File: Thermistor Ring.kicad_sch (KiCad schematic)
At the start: 20 parts, among them IC1 MAX30210ENL+, IC2 MAX30210ENL+, IC3 MAX30210ENL+, IC4 MAX30210ENL+, IC5 MAX30210ENL+, IC6 MAX30210ENL+, J1 Conn_01x04_Socket, J3 Conn_01x03_Socket, U1 TPS7A2018PDBVR

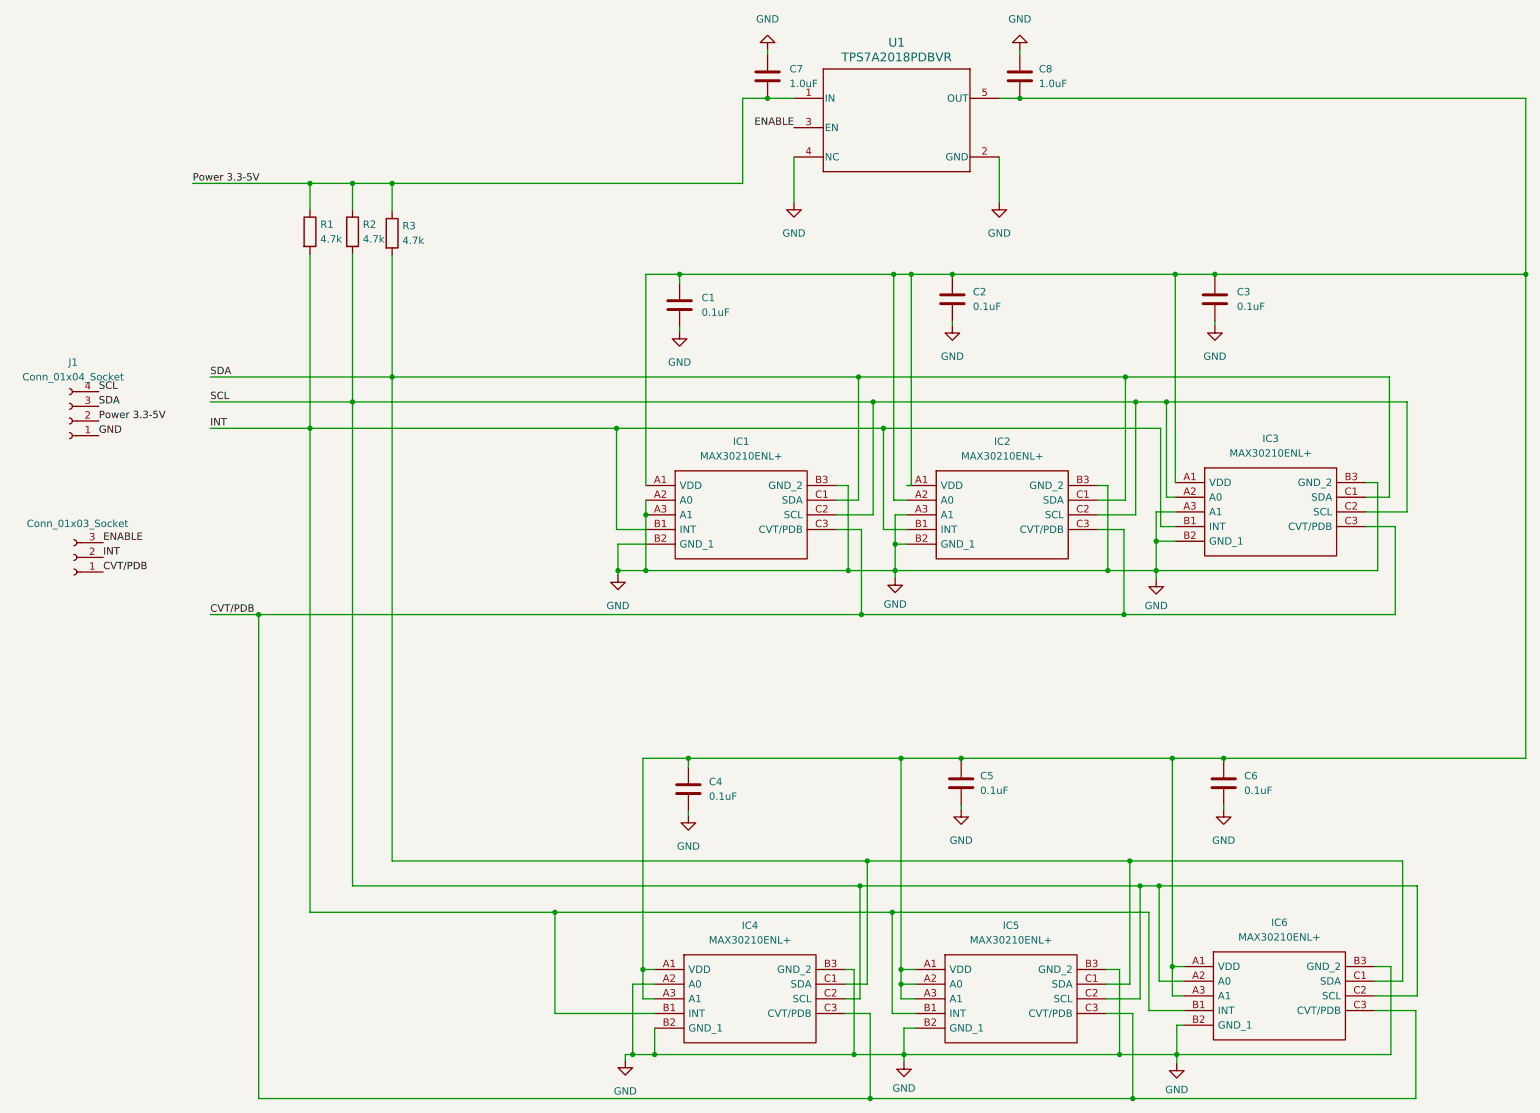
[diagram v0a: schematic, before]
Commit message: footprints added to schematic
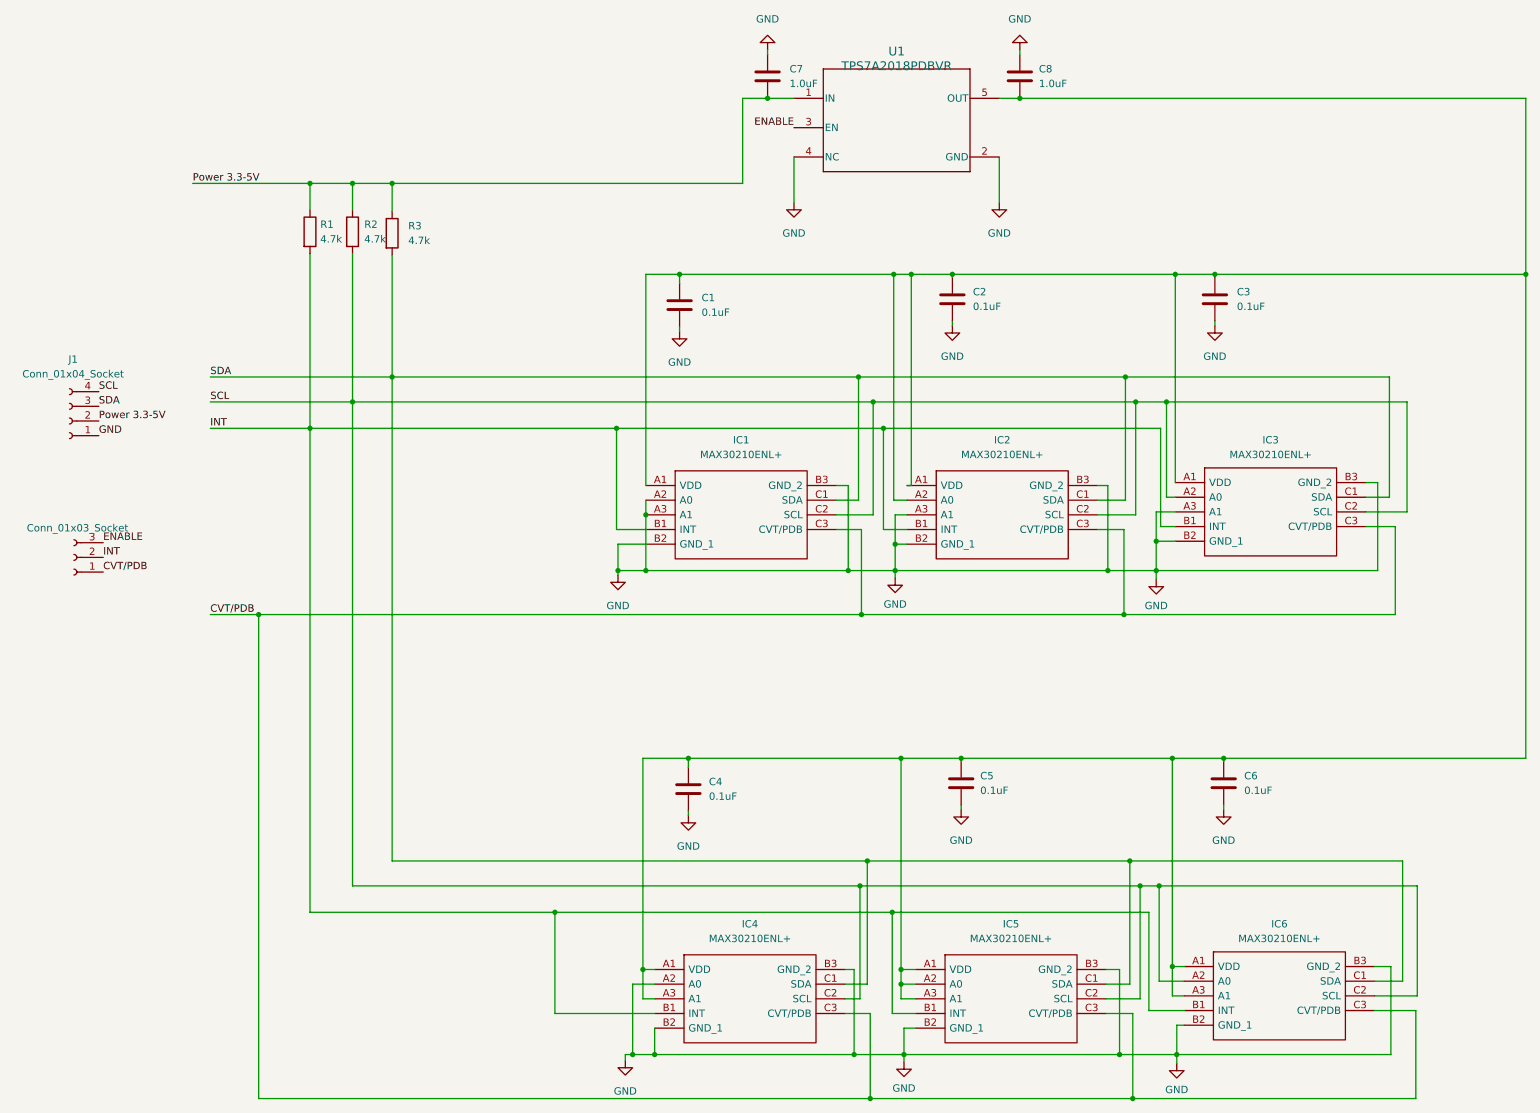
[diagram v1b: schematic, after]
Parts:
- C1, C2, C3, C4, C5, C6, C7, C8: footprint (none) -> Capacitor_SMD:C_0805_2012Metric
- IC1, IC2, IC3, IC4, IC5, IC6: footprint BGA9C30P3X3_97X97X50 -> MAX30210:21-100600_N90A0&plus_1_ADI
- J1: footprint (none) -> Connector_JST:JST_XH_B4B-XH-A_1x04_P2.50mm_Vertical
- J3: footprint (none) -> Connector_JST:JST_XH_B3B-XH-A_1x03_P2.50mm_Vertical
- R1, R2, R3: footprint (none) -> Resistor_SMD:R_0805_2012Metric
- U1: footprint DBV0005A-IPC_A -> LDO_TSA7A:DBV0005A-IPC_A

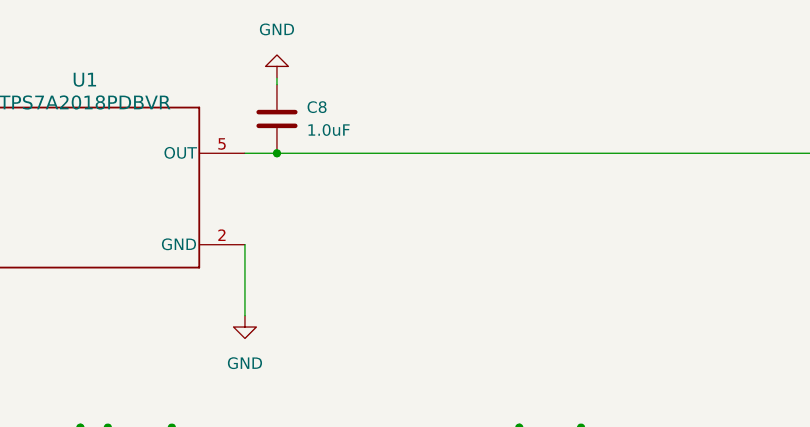
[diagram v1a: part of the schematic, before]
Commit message: saving before moving thermistors
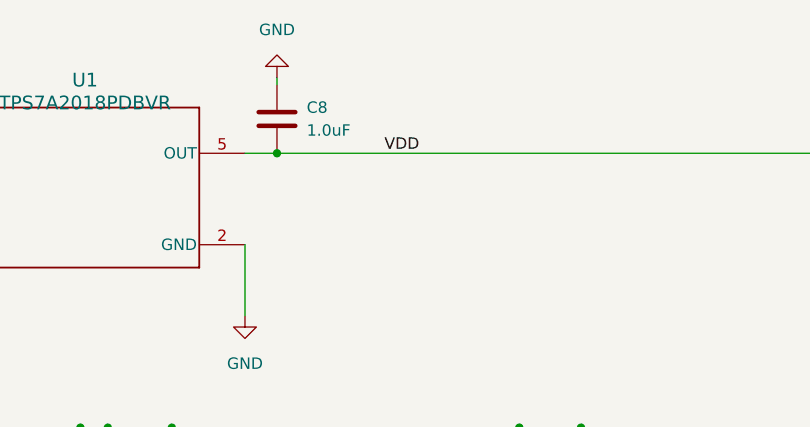
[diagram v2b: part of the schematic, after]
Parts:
- C5, C6, C7, C8: footprint Capacitor_SMD:C_0805_2012Metric -> Capacitor_SMD:C_0603_1608Metric
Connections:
- net VDD: now reaches C1.1, C2.1, C3.1, C4.1, C5.1, C6.1, C8.1, IC1.A1 (VDD), IC2.A1 (VDD), IC2.A2 (A0), IC3.A1 (VDD), IC4.A1 (VDD), IC4.A3 (A1), IC5.A1 (VDD), IC5.A2 (A0), IC5.A3 (A1), IC6.A1 (VDD), IC6.A3 (A1), U1.5 (OUT)
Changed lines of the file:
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@@
+    (effects (font (size 1.27 1.27)) (justify left bottom))
+  )
+  (label "VDD" (at 152.146 -12.192 0) (fields_autoplaced)
     (effects (font (size 1.27 1.27)) (justify left bottom))
   )
@@
       (effects (font (size 1.27 1.27)) (justify right))
     )
-    (property "Footprint" "Capacitor_SMD:C_0805_2012Metric" (at 139.2428 -19.812 0)
+    (property "Footprint" "Capacitor_SMD:C_0603_1608Metric" (at 139.2428 -19.812 0)
       (effects (font (size 1.27 1.27)) hide)
     )
@@
       (effects (font (size 1.27 1.27)) (justify left))
     )
-    (property "Footprint" "Capacitor_SMD:C_0805_2012Metric" (at 131.0132 110.236 0)
+    (property "Footprint" "Capacitor_SMD:C_0603_1608Metric" (at 131.0132 110.236 0)
       (effects (font (size 1.27 1.27)) hide)
     )
@@
       (effects (font (size 1.27 1.27)) (justify right))
     )
-    (property "Footprint" "Capacitor_SMD:C_0805_2012Metric" (at 95.5548 -19.812 0)
+    (property "Footprint" "Capacitor_SMD:C_0603_1608Metric" (at 95.5548 -19.812 0)
       (effects (font (size 1.27 1.27)) hide)
     )
@@
       (effects (font (size 1.27 1.27)) (justify left))
     )
-    (property "Footprint" "Capacitor_SMD:C_0805_2012Metric" (at 176.4792 110.236 0)
-      (effects (font (size 1.27 1.27)) hide)
-    )
+    (property "Footprint" "Capacitor_SMD:C_0603_1608Metric" (at 176.4792 110.236 0)
+      (effects (font (size 1.27 1.27)) hide)
+    )
